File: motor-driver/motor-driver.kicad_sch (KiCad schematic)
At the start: 48 parts, among them Q1 NMOS, Q2 NMOS, Q3 NMOS, Q4 NMOS, Q5 NMOS, Q6 NMOS, U3 FAN7388

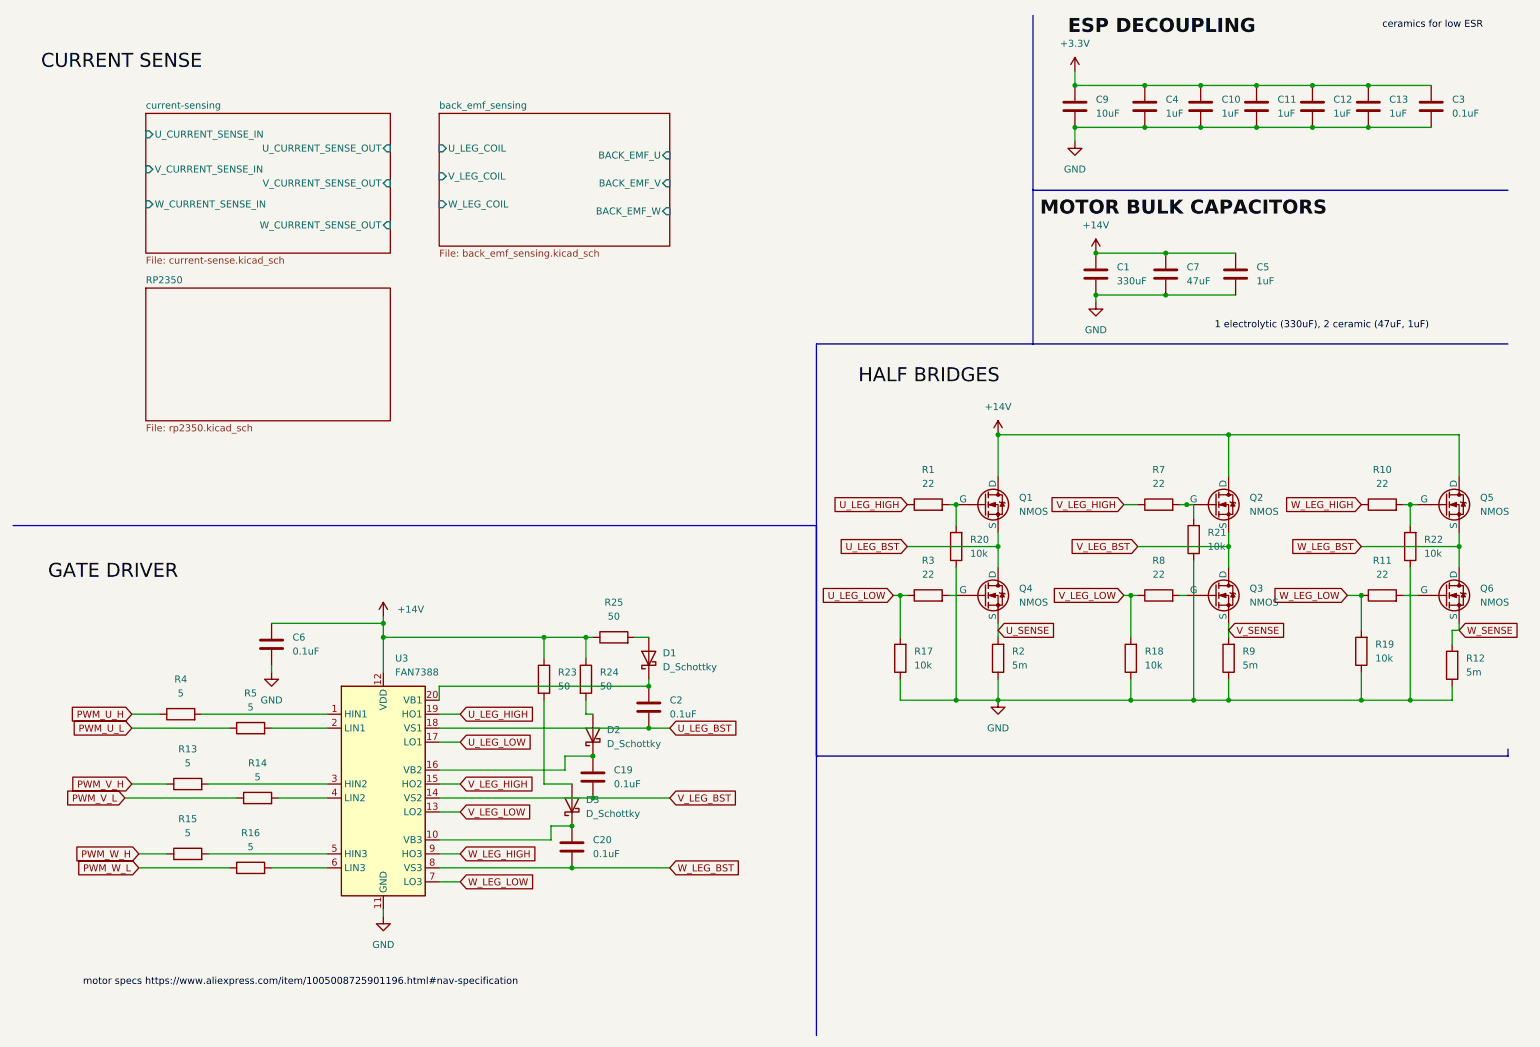
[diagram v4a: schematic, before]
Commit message: completed sheet connections
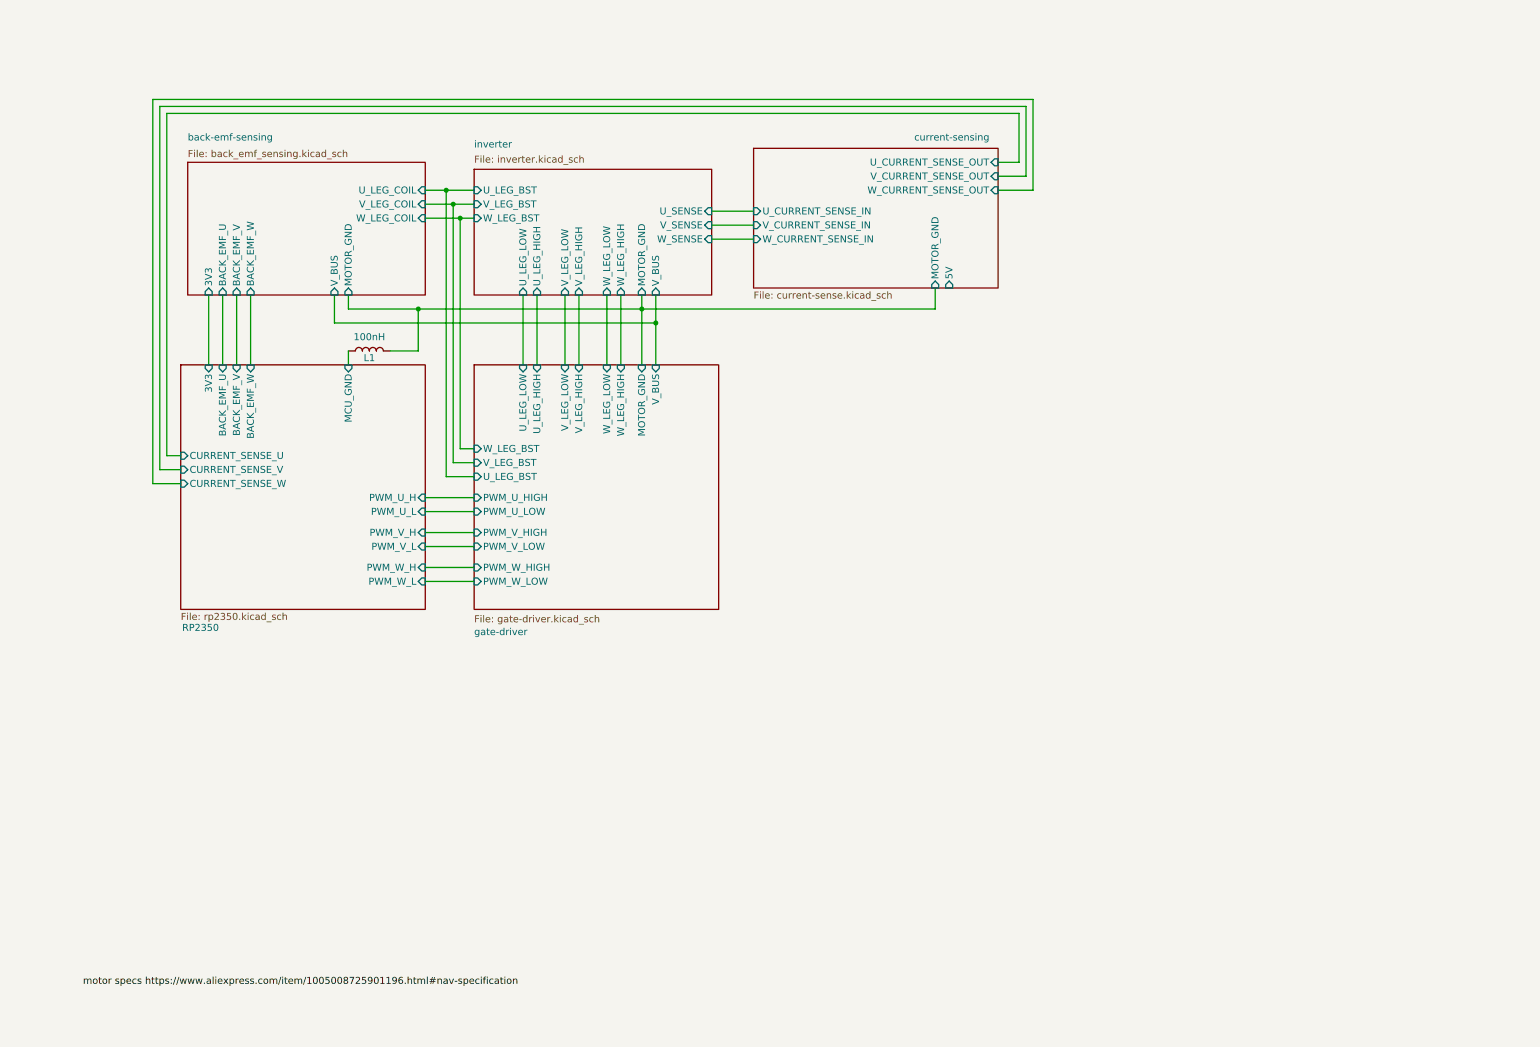
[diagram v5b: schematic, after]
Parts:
- removed C1: 330uF, Capacitor_SMD:C_0201_0603Metric_Pad0.64x0.40mm_HandSolder, symbol Device:C
- removed C10, C11, C12, C13, C4: 1uF, Capacitor_SMD:C_0603_1608Metric, symbol Device:C
- removed C19, C2, C20: 0.1uF, Capacitor_SMD:C_0201_0603Metric_Pad0.64x0.40mm_HandSolder, symbol Device:C
- removed C3: 0.1uF, Capacitor_SMD:C_0603_1608Metric, symbol Device:C
- removed C5: 1uF, Capacitor_SMD:C_0201_0603Metric_Pad0.64x0.40mm_HandSolder, symbol Device:C
- removed C6: 0.1uF, Capacitor_SMD:C_0603_1608Metric_Pad1.08x0.95mm_HandSolder, symbol Device:C
- removed C7: 47uF, Capacitor_SMD:C_0201_0603Metric_Pad0.64x0.40mm_HandSolder, symbol Device:C
- removed C9: 10uF, Capacitor_SMD:C_0603_1608Metric, symbol Device:C
- removed D1, D2, D3: D_Schottky, Diode_SMD:D_0201_0603Metric_Pad0.64x0.40mm_HandSolder, symbol Device:D_Schottky
- removed Q1, Q2, Q3, Q4, Q5, Q6: NMOS, symbol Simulation_SPICE:NMOS
- removed R1, R10, R11, R3, R7, R8: 22, symbol Device:R
- removed R12, R2, R9: 5m, symbol Device:R
- removed R13, R14, R15, R16, R4, R5: 5, symbol Device:R
- removed R17, R18, R19, R20, R21, R22: 10k, symbol Device:R
- removed R23, R24, R25: 50, symbol Device:R
- removed U3: FAN7388, Package_SO:SOIC-20W_7.5x12.8mm_P1.27mm, symbol Driver_FET:FAN7388
- added L1: 100nH, symbol Device:L
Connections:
- new net RP2350/MCU_GND: L1.1
- new net back-emf-sensing/MOTOR_GND: L1.2
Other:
- sheet back_emf_sensing renamed back-emf-sensing
- added sheet gate-driver (gate-driver.kicad_sch)
- added sheet inverter (inverter.kicad_sch)
- sheet RP2350 ports: added 3V3, BACK_EMF_U, BACK_EMF_V, BACK_EMF_W, CURRENT_SENSE_U, CURRENT_SENSE_V, CURRENT_SENSE_W, MCU_GND, PWM_U_H, PWM_U_L, PWM_V_H, PWM_V_L, PWM_W_H, PWM_W_L; removed none
- sheet back-emf-sensing ports: added 3V3, MOTOR_GND, V_BUS; removed none
- sheet current-sensing ports: added 5V, MOTOR_GND; removed none

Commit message: added connectors starting pcb layout
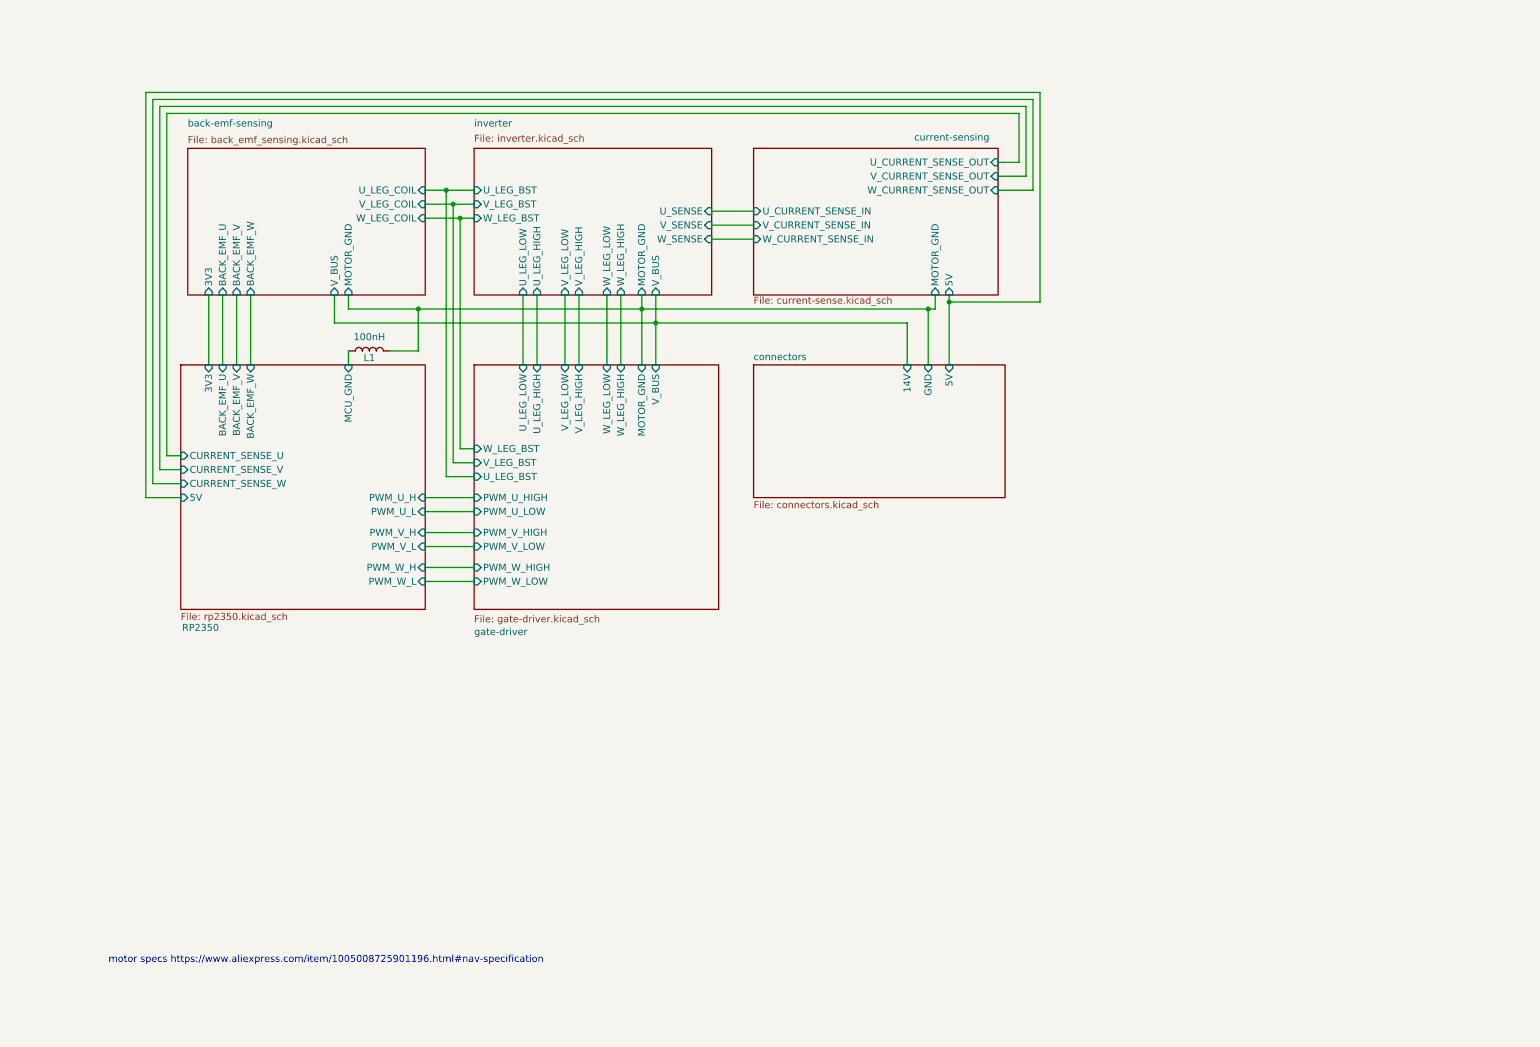
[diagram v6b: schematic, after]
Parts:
- L1: footprint (none) -> Inductor_SMD:L_0805_2012Metric
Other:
- added sheet connectors (connectors.kicad_sch)
- sheet RP2350 ports: added 5V; removed none
- note added: "motor specs https://www.aliexpress.com/item/1005008725901196.html#nav-specification"
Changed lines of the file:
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@@
 	(generator_version "9.0")
 	(paper "A4")
+	(text "motor specs https://www.aliexpress.com/item/1005008725901196.html#nav-specification"
+		(exclude_from_sim no)
+		(at 69.596 184.404 0)
+		(effects
+			(font
+				(size 1.27 1.27)
+			)
+		)
+	)
+	(junction
+		(at 182.88 64.77)
+		(diameter 0)
+		(color 0 0 0 0)
+	)
 	(junction
 		(at 93.98 49.53)
@@
 	)
 	(junction
+		(at 179.07 66.04)
+		(diameter 0)
+		(color 0 0 0 0)
+	)
+	(junction
 		(at 129.54 68.58)
 		(diameter 0)
@@
 	(wire
 		(pts
+			(xy 179.07 66.04) (xy 179.07 76.2)
+		)
+		(stroke
+			(width 0)
+			(type default)
+		)
+	)
+	(wire
+		(pts
 			(xy 198.12 44.45) (xy 198.12 27.94)
 		)
@@
 	(wire
 		(pts
+			(xy 36.83 26.67) (xy 36.83 100.33)
+		)
+		(stroke
+			(width 0)
+			(type default)
+		)
+	)
+	(wire
+		(pts
 			(xy 71.12 68.58) (xy 129.54 68.58)
 		)
@@
 	(wire
 		(pts
+			(xy 36.83 26.67) (xy 199.39 26.67)
+		)
+		(stroke
+			(width 0)
+			(type default)
+		)
+	)
+	(wire
+		(pts
 			(xy 105.41 63.5) (xy 105.41 76.2)
 		)
@@
 	(wire
 		(pts
-			(xy 180.34 62.23) (xy 180.34 66.04)
-		)
-		(stroke
-			(width 0)
-			(type default)
-		)
-	)
-	(wire
-		(pts
 			(xy 120.65 63.5) (xy 120.65 76.2)
 		)
@@
 	(wire
 		(pts
+			(xy 182.88 64.77) (xy 182.88 76.2)
+		)
+		(stroke
+			(width 0)
+			(type default)
+		)
+	)
+	(wire
+		(pts
 			(xy 92.71 46.99) (xy 92.71 93.98)
 		)
@@
 	(wire
 		(pts
+			(xy 180.34 63.5) (xy 180.34 66.04)
+		)
+		(stroke
+			(width 0)
+			(type default)
+		)
+	)
+	(wire
+		(pts
 			(xy 196.85 29.21) (xy 39.37 29.21)
 		)
@@
 	(wire
 		(pts
+			(xy 43.18 100.33) (xy 36.83 100.33)
+		)
+		(stroke
+			(width 0)
+			(type default)
+		)
+	)
+	(wire
+		(pts
 			(xy 139.7 50.8) (xy 147.32 50.8)
 		)
@@
 	(wire
 		(pts
-			(xy 180.34 66.04) (xy 127 66.04)
+			(xy 180.34 66.04) (xy 179.07 66.04)
 		)
 		(stroke
@@
 	(wire
 		(pts
+			(xy 175.26 76.2) (xy 175.26 68.58)
+		)
+		(stroke
+			(width 0)
+			(type default)
+		)
+	)
+	(wire
+		(pts
 			(xy 50.8 63.5) (xy 50.8 76.2)
 		)
@@
 	(wire
 		(pts
+			(xy 129.54 68.58) (xy 175.26 68.58)
+		)
+		(stroke
+			(width 0)
+			(type default)
+		)
+	)
+	(wire
+		(pts
 			(xy 87.63 44.45) (xy 91.44 44.45)
 		)
@@
 	(wire
 		(pts
+			(xy 182.88 64.77) (xy 182.88 63.5)
+		)
+		(stroke
+			(width 0)
+			(type default)
+		)
+	)
+	(wire
+		(pts
 			(xy 40.64 30.48) (xy 40.64 92.71)
 		)
@@
 	(wire
 		(pts
+			(xy 179.07 66.04) (xy 127 66.04)
+		)
+		(stroke
+			(width 0)
+			(type default)
+		)
+	)
+	(wire
+		(pts
 			(xy 87.63 46.99) (xy 92.71 46.99)
 		)
@@
 	(wire
 		(pts
+			(xy 182.88 64.77) (xy 199.39 64.77)
+		)
+		(stroke
+			(width 0)
+			(type default)
+		)
+	)
+	(wire
+		(pts
+			(xy 199.39 26.67) (xy 199.39 64.77)
+		)
+		(stroke
+			(width 0)
+			(type default)
+		)
+	)
+	(wire
+		(pts
 			(xy 87.63 106.68) (xy 96.52 106.68)
 		)
@@
 			(width 0)
 			(type default)
-		)
-	)
-	(label "motor specs https:{slash}{slash}www.aliexpress.com{slash}item{slash}1005008725901196.html#nav-specification"
-		(at 25.4 189.23 0)
-		(effects
-			(font
-				(size 1.27 1.27)
-			)
-			(justify left bottom)
 		)
 	)
@@
 			)
 		)
-		(property "Footprint" ""
+		(property "Footprint" "Inductor_SMD:L_0805_2012Metric"
 			(at 77.47 73.66 0)
 			(effects
@@
 	)
 	(sheet
-		(at 44.45 39.37)
-		(size 43.18 24.13)
+		(at 44.45 36.83)
+		(size 43.18 26.67)
 		(exclude_from_sim no)
 		(in_bom yes)
@@
 		)
 		(property "Sheetname" "back-emf-sensing"
-			(at 44.45 35.56 0)
+			(at 44.45 33.02 0)
 			(effects
 				(font
@@
 		)
 		(property "Sheetfile" "back_emf_sensing.kicad_sch"
-			(at 44.45 37.084 0)
+			(at 44.45 34.544 0)
 			(effects
 				(font
@@
 				(path "/2980fc7e-b297-4843-ba9f-cceafa384b2f"
 					(page "2")
+				)
+			)
+		)
+	)
+	(sheet
+		(at 147.32 76.2)
+		(size 45.72 24.13)
+		(exclude_from_sim no)
+		(in_bom yes)
+		(on_board yes)
+		(dnp no)
+		(fields_autoplaced yes)
+		(stroke
+			(width 0.1524)
+			(type solid)
+		)
+		(fill
+			(color 0 0 0 0.0000)
+		)
+		(property "Sheetname" "connectors"
+			(at 147.32 75.4884 0)
+			(effects
+				(font
+					(size 1.27 1.27)
+				)
+				(justify left bottom)
+			)
+		)
+		(property "Sheetfile" "connectors.kicad_sch"
+			(at 147.32 100.9146 0)
+			(effects
+				(font
+					(size 1.27 1.27)
+				)
+				(justify left top)
+			)
+		)
+		(pin "5V" input
+			(at 182.88 76.2 90)
+			(effects
+				(font
+					(size 1.27 1.27)
+				)
+				(justify right)
+			)
+		)
+		(pin "14V" input
+			(at 175.26 76.2 90)
+			(effects
+				(font
+					(size 1.27 1.27)
+				)
+				(justify right)
+			)
+		)
+		(pin "GND" input
+			(at 179.07 76.2 90)
+			(effects
+				(font
+					(size 1.27 1.27)
+				)
+				(justify right)
+			)
+		)
+		(instances
+			(project "motor-driver"
+				(path "/2980fc7e-b297-4843-ba9f-cceafa384b2f"
+					(page "7")
 				)
 			)
@@
 	(sheet
 		(at 147.32 36.83)
-		(size 44.45 25.4)
+		(size 44.45 26.67)
 		(exclude_from_sim no)
 		(in_bom yes)
@@
 		)
 		(property "Sheetfile" "current-sense.kicad_sch"
-			(at 147.32 62.8146 0)
+			(at 147.32 63.754 0)
 			(effects
 				(font
@@
 		)
 		(pin "5V" input
-			(at 182.88 62.23 270)
+			(at 182.88 63.5 270)
 			(effects
 				(font
@@
 		)
 		(pin "MOTOR_GND" input
-			(at 180.34 62.23 270)
+			(at 180.34 63.5 270)
 			(effects
 				(font
@@
 	)
 	(sheet
-		(at 96.52 40.64)
-		(size 43.18 22.86)
+		(at 96.52 36.83)
+		(size 43.18 26.67)
 		(exclude_from_sim no)
 		(in_bom yes)
@@
 		)
 		(property "Sheetname" "inverter"
-			(at 96.52 36.83 0)
+			(at 96.52 33.02 0)
 			(effects
 				(font
@@
 		)
 		(property "Sheetfile" "inverter.kicad_sch"
-			(at 96.52 38.1 0)
+			(at 96.52 34.29 0)
 			(effects
 				(font
@@
 			)
 		)
+		(pin "5V" input
+			(at 43.18 100.33 180)
+			(effects
+				(font
+					(size 1.27 1.27)
+				)
+				(justify left)
+			)
+		)

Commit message: post revisions
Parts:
- removed L1: 100nH, Inductor_SMD:L_0805_2012Metric, symbol Device:L
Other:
- removed sheet back-emf-sensing
- removed sheet current-sensing
- removed sheet gate-driver
- sheet RP2350 ports: added USB_D+, USB_D-; removed 3V3, 5V, MCU_GND
- sheet connectors ports: added USB_D+, USB_D-; removed 14V, 5V, GND
- sheet inverter ports: added BEMF_U, BEMF_V, BEMF_W, CURRENT_SENSE_U, CURRENT_SENSE_V, CURRENT_SENSE_W, PWM_UH, PWM_UL, PWM_VH, PWM_VL, PWM_WH, PWM_WL; removed MOTOR_GND, U_LEG_BST, U_LEG_HIGH, U_LEG_LOW, U_SENSE, V_BUS, V_LEG_BST, V_LEG_HIGH, V_LEG_LOW, V_SENSE, W_LEG_BST, W_LEG_HIGH, W_LEG_LOW, W_SENSE
- company: (none) -> Drone 

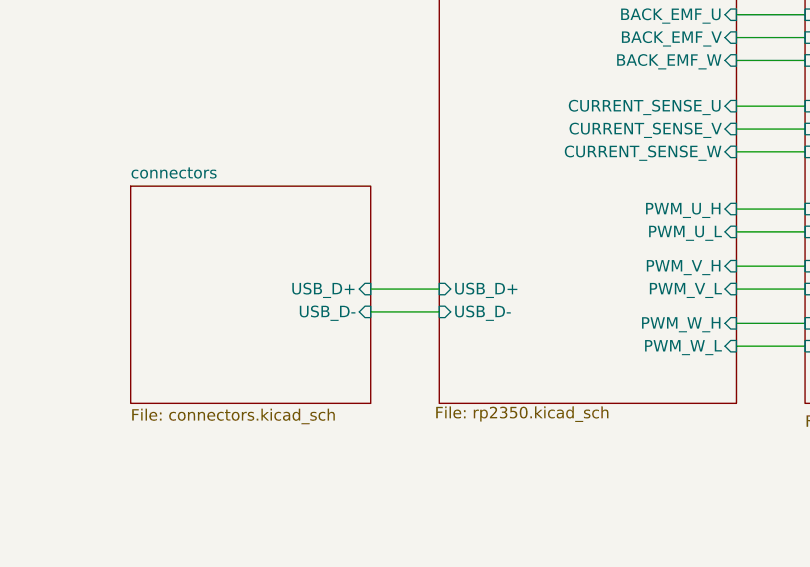
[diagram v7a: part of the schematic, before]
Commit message: added spi connection
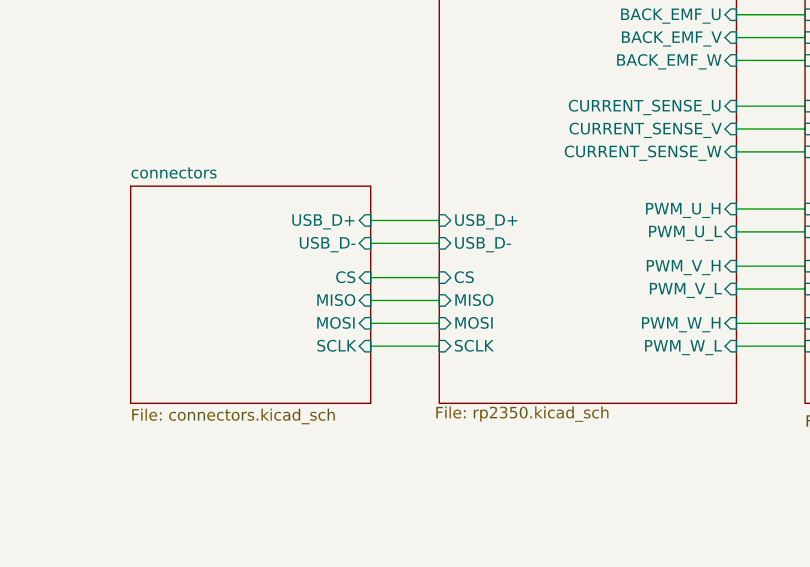
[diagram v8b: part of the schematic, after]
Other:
- sheet RP2350 ports: added CS, MISO, MOSI, SCLK; removed none
- sheet connectors ports: added CS, MISO, MOSI, SCLK; removed none
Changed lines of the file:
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@@
 	(wire
 		(pts
-			(xy 105.41 106.68) (xy 113.03 106.68)
+			(xy 105.41 110.49) (xy 113.03 110.49)
+		)
+		(stroke
+			(width 0)
+			(type default)
+		)
+	)
+	(wire
+		(pts
+			(xy 105.41 99.06) (xy 113.03 99.06)
 		)
 		(stroke
@@
 	(wire
 		(pts
+			(xy 105.41 113.03) (xy 113.03 113.03)
+		)
+		(stroke
+			(width 0)
+			(type default)
+		)
+	)
+	(wire
+		(pts
+			(xy 105.41 105.41) (xy 113.03 105.41)
+		)
+		(stroke
+			(width 0)
+			(type default)
+		)
+	)
+	(wire
+		(pts
 			(xy 146.05 88.9) (xy 153.67 88.9)
 		)
@@
 	(wire
 		(pts
-			(xy 105.41 109.22) (xy 113.03 109.22)
+			(xy 105.41 101.6) (xy 113.03 101.6)
+		)
+		(stroke
+			(width 0)
+			(type default)
+		)
+	)
+	(wire
+		(pts
+			(xy 105.41 107.95) (xy 113.03 107.95)
 		)
 		(stroke
@@
 		)
 		(pin "USB_D+" input
-			(at 105.41 106.68 0)
+			(at 105.41 99.06 0)
 			(effects
 				(font
@@
 		)
 		(pin "USB_D-" input
-			(at 105.41 109.22 0)
+			(at 105.41 101.6 0)
+			(effects
+				(font
+					(size 1.27 1.27)
+				)
+				(justify right)
+			)
+		)
+		(pin "CS" input
+			(at 105.41 105.41 0)
+			(effects
+				(font
+					(size 1.27 1.27)
+				)
+				(justify right)
+			)
+		)
+		(pin "MISO" input
+			(at 105.41 107.95 0)
+			(effects
+				(font
+					(size 1.27 1.27)
+				)
+				(justify right)
+			)
+		)
+		(pin "MOSI" input
+			(at 105.41 110.49 0)
+			(effects
+				(font
+					(size 1.27 1.27)
+				)
+				(justify right)
+			)
+		)
+		(pin "SCLK" input
+			(at 105.41 113.03 0)
 			(effects
 				(font
@@
 		)
 		(pin "USB_D+" input
-			(at 113.03 106.68 180)
+			(at 113.03 99.06 180)
 			(effects
 				(font
@@
 		)
 		(pin "USB_D-" input
-			(at 113.03 109.22 180)
-			(effects
-				(font
+			(at 113.03 101.6 180)
+			(effects
+				(font
+					(size 1.27 1.27)
+				)
+				(justify left)
+			)
+		)
+		(pin "CS" input
+			(at 113.03 105.41 180)
+			(effects
+				(font
+					(size 1.27 1.27)
+				)
+				(justify left)
+			)
+		)
+		(pin "MISO" input
+			(at 113.03 107.95 180)
+			(effects
+				(font
+					(size 1.27 1.27)
+				)
+				(justify left)
+			)
+		)
+		(pin "MOSI" input
+			(at 113.03 110.49 180)
+			(effects
+				(font
+					(size 1.27 1.27)
+				)
+				(justify left)
+			)
+		)
+		(pin "SCLK" input
+			(at 113.03 113.03 180)
+			(effects
+				(font
